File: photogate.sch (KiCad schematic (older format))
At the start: 22 parts, among them P1 CONN_01X02, P10 CONN_01X01, P11 CONN_01X01, P2 CONN_01X02, P3 CONN_01X01, P4 CONN_02X05, P5 CONN_02X04, P6 CONN_01X02, P7 CONN_02X05, P8 CONN_01X02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

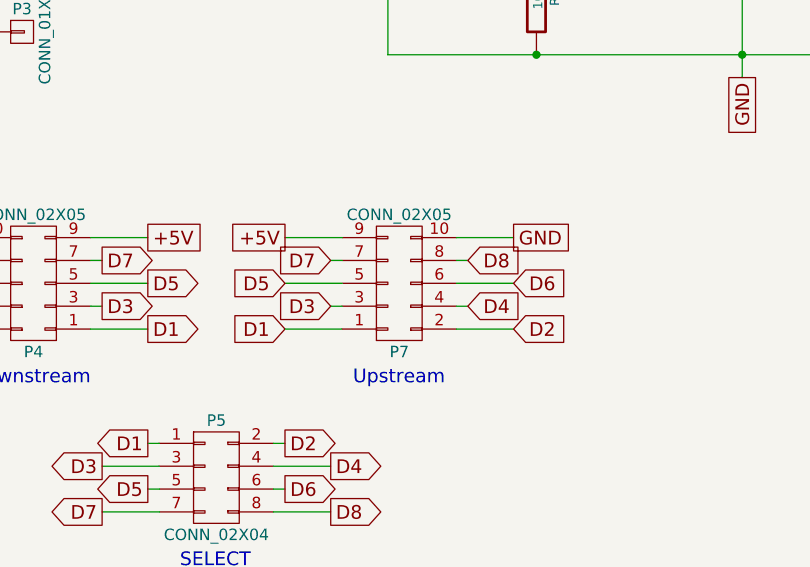
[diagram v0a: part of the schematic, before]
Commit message: Flipped flat cable connector
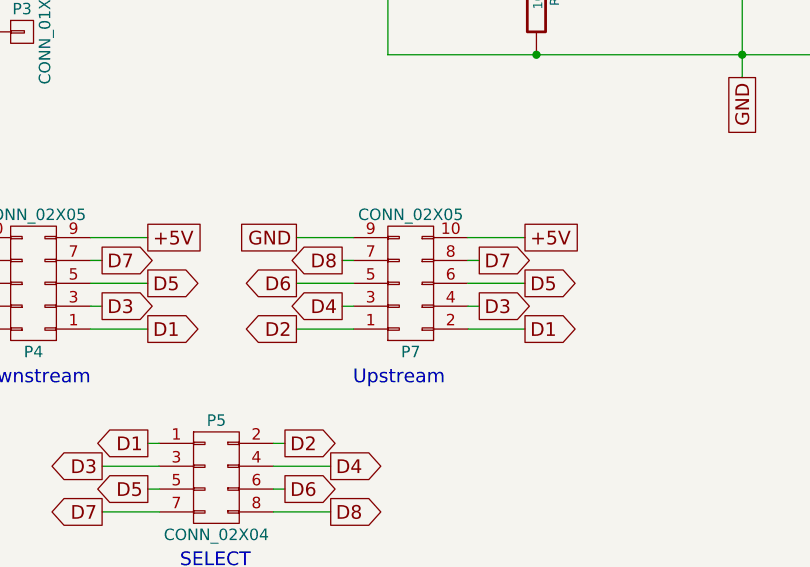
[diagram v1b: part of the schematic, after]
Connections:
- net +5V: now also P7.10 (P10); no longer P7.9 (P9)
- net D1: now also P7.2 (P2); no longer P7.1 (P1)
- net D2: now also P7.1 (P1); no longer P7.2 (P2)
- net D3: now also P7.4 (P4); no longer P7.3 (P3)
- net D4: now also P7.3 (P3); no longer P7.4 (P4)
- net D5: now also P7.6 (P6); no longer P7.5 (P5)
- net D6: now also P7.5 (P5); no longer P7.6 (P6)
- net D7: now also P7.8 (P8); no longer P7.7 (P7)
- net D8: now also P7.7 (P7); no longer P7.8 (P8)
- net GND: now also P7.9 (P9); no longer P7.10 (P10)
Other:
- moved on the sheet: P7
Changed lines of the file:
@@
 	-1   0    0    1
 $EndComp
-Text GLabel 7300 3400 2    60   UnSpc ~ 0
-GND
-Text GLabel 6300 3400 0    60   UnSpc ~ 0
-+5V
 Text GLabel 4700 3800 0    60   Output ~ 0
 D2
@@
 L CONN_02X05 P7
 U 1 1 5421918E
-P 6800 3600
-F 0 "P7" H 6800 3900 50  0000 C CNN
-F 1 "CONN_02X05" H 6800 3300 50  0000 C CNN
-F 2 "Socket_Strips:Socket_Strip_Straight_2x05" H 6800 2400 60  0001 C CNN
-F 3 "" H 6800 2400 60  0000 C CNN
-	1    6800 3600
+P 6850 3600
+F 0 "P7" H 6850 3900 50  0000 C CNN
+F 1 "CONN_02X05" H 6850 3300 50  0000 C CNN
+F 2 "Socket_Strips:Socket_Strip_Straight_2x05" H 6850 2400 60  0001 C CNN
+F 3 "" H 6850 2400 60  0000 C CNN
+	1    6850 3600
 	1    0    0    1
 $EndComp
@@
 Text GLabel 5700 3400 2    60   UnSpc ~ 0
 +5V
-Text GLabel 7300 3800 2    60   Input ~ 0
-D2
-Text GLabel 7100 3700 2    60   Input ~ 0
-D4
-Text GLabel 7300 3600 2    60   Input ~ 0
-D6
-Text GLabel 7100 3500 2    60   Input ~ 0
-D8
-Text GLabel 6300 3800 0    60   Input ~ 0
-D1
-Text GLabel 6500 3700 0    60   Input ~ 0
-D3
-Text GLabel 6300 3600 0    60   Input ~ 0
-D5
-Text GLabel 6500 3500 0    60   Input ~ 0
-D7
 Text Notes 7000 4050 2    60   ~ 0
 Upstream
@@
 Wire Wire Line
 	4900 1900 5000 1900
-Wire Wire Line
-	6500 3500 6550 3500
-Wire Wire Line
-	6300 3600 6550 3600
-Wire Wire Line
-	6550 3700 6500 3700
-Wire Wire Line
-	6300 3800 6550 3800
-Wire Wire Line
-	7100 3700 7050 3700
-Wire Wire Line
-	7300 3800 7050 3800
-Wire Wire Line
-	7050 3500 7100 3500
-Wire Wire Line
-	7300 3600 7050 3600
 Connection ~ 2800 2000
 Wire Wire Line
@@
 Wire Wire Line
 	5450 3400 5700 3400
-Wire Wire Line
-	6300 3400 6550 3400
-Wire Wire Line
-	7050 3400 7300 3400
+Text GLabel 7350 3800 2    60   Output ~ 0
+D1
+Text GLabel 7150 3700 2    60   Output ~ 0
+D3
+Text GLabel 7350 3600 2    60   Output ~ 0
+D5
+Text GLabel 7150 3500 2    60   Output ~ 0
+D7
+Text GLabel 7350 3400 2    60   UnSpc ~ 0
++5V
+Wire Wire Line
+	7100 3800 7350 3800
+Wire Wire Line
+	7100 3700 7150 3700
+Wire Wire Line
+	7100 3600 7350 3600
+Wire Wire Line
+	7100 3500 7150 3500
+Wire Wire Line
+	7100 3400 7350 3400
+Text GLabel 6350 3800 0    60   Output ~ 0
+D2
+Text GLabel 6550 3700 0    60   Output ~ 0
+D4
+Text GLabel 6350 3600 0    60   Output ~ 0
+D6
+Text GLabel 6550 3500 0    60   Output ~ 0
+D8
+Text GLabel 6350 3400 0    60   UnSpc ~ 0
+GND
+Wire Wire Line
+	6350 3600 6600 3600
+Wire Wire Line
+	6350 3800 6600 3800
+Wire Wire Line
+	6350 3400 6600 3400
+Wire Wire Line
+	6550 3500 6600 3500
+Wire Wire Line
+	6600 3700 6550 3700
 $EndSCHEMATC

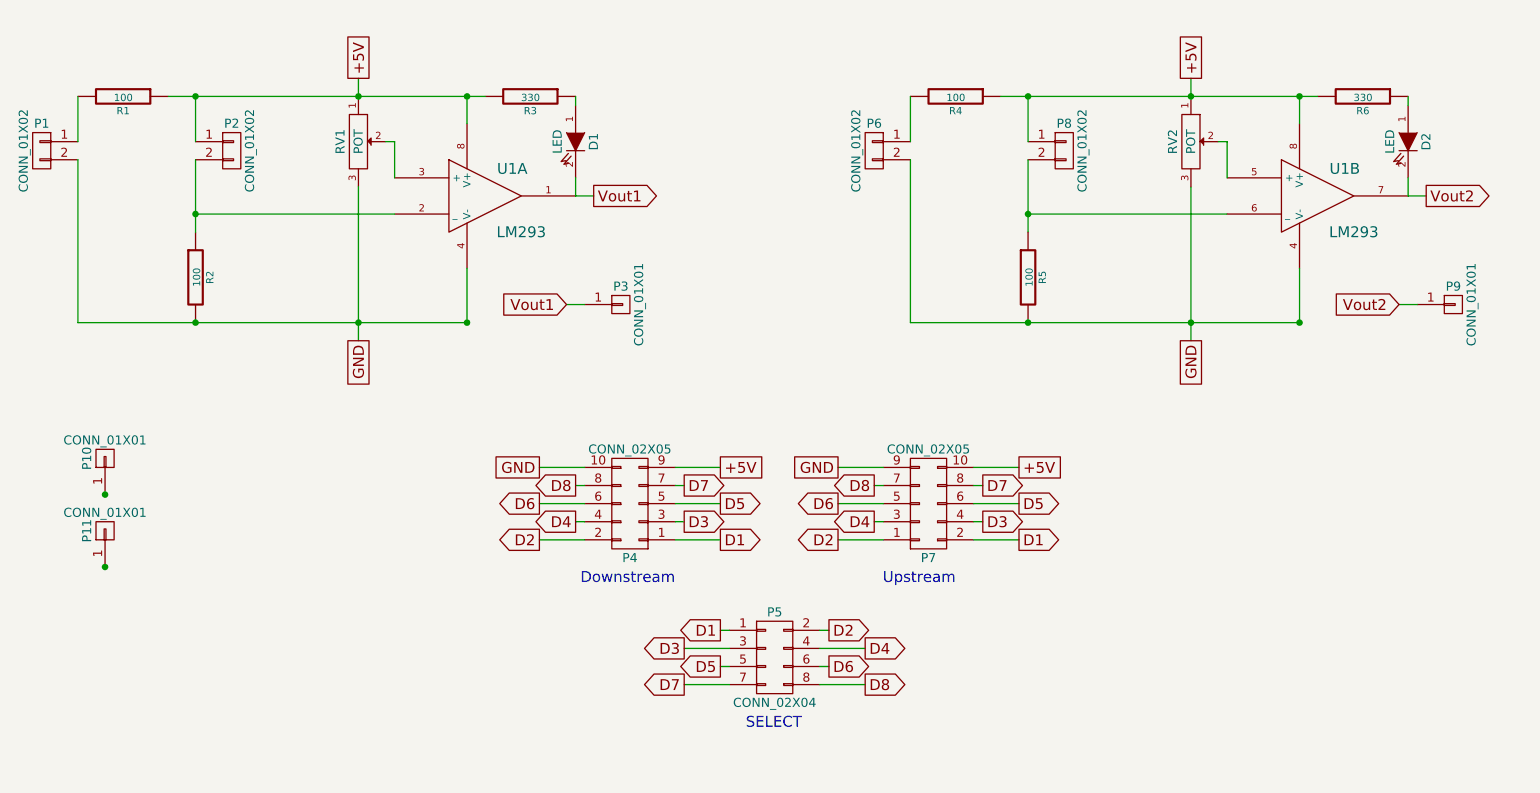
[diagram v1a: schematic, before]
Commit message: Rebuild layout w/ updated footprints
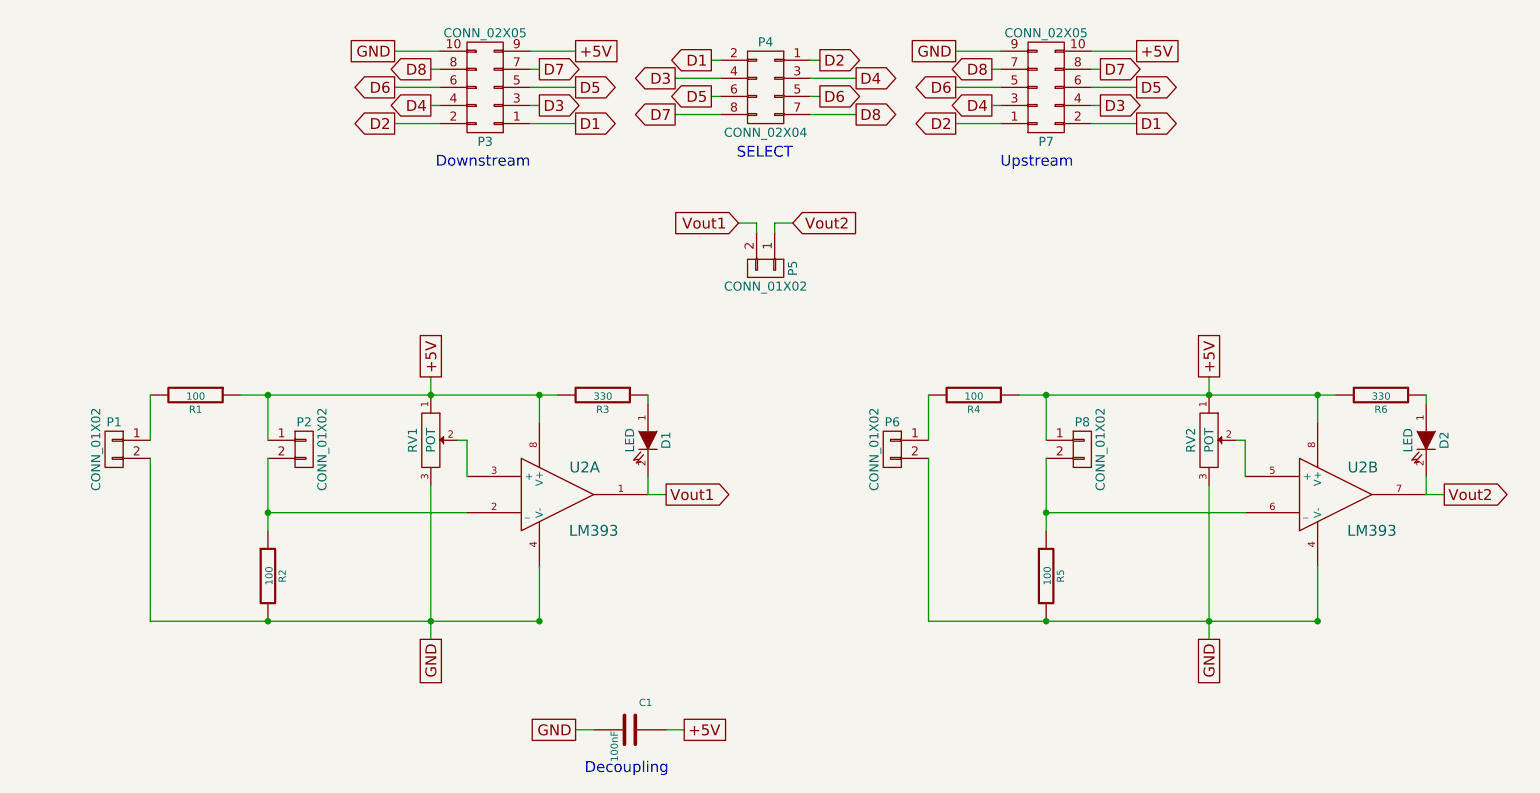
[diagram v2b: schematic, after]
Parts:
- removed P10, P11: CONN_01X01, Mounting_Holes:MountingHole_5mm, symbol CONN_01X01
- removed P3, P9: CONN_01X01, Socket_Strips:Socket_Strip_Straight_1x01, symbol CONN_01X01
- removed U1: LM293, Sockets_DIP:DIP-8__300, symbol LM293
- added C1: 100nF, SMD_Packages:SMD-1206, symbol C
- added P5: CONN_01X02, Socket_Strips:Socket_Strip_Straight_1x02, symbol CONN_01X02
- added U2: LM393, Sockets_DIP:DIP-8__300, symbol LM393
- P3: renamed from P4; footprint Socket_Strips:Socket_Strip_Straight_2x05 -> photogate_mods:Wurth_2x05_HEADER_STRAIGHT
- P7: footprint Socket_Strips:Socket_Strip_Straight_2x05 -> photogate_mods:Wurth_2x05_HEADER_STRAIGHT
- R1, R2, R3, R4, R5, R6: footprint Resistors_SMD:R_1206_HandSoldering -> Resistors_SMD:R_1206
- RV1, RV2: footprint Potentiometers:Potentiometer_Triwood_RM-065 -> photogate_mods:PVZ2A
- renumbered P5 to P4
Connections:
- net +5V: now also C1.1, U2.8 (V+), U2.8 (V+)
- net D1: now also P4.2 (P2); no longer P4.1 (P1)
- net D2: now also P4.1 (P1); no longer P4.2 (P2)
- net D3: now also P4.4 (P4); no longer P4.3 (P3)
- net D4: now also P4.3 (P3); no longer P4.4 (P4)
- net D5: now also P4.6 (P6); no longer P4.5 (P5)
- net D6: now also P4.5 (P5); no longer P4.6 (P6)
- net D7: now also P4.8 (P8); no longer P4.7 (P7)
- net D8: now also P4.7 (P7); no longer P4.8 (P8)
- net GND: now also C1.2, U2.4 (V-), U2.4 (V-)
- net Vout1: now also P5.2 (P2), U2.1
- net Vout2: now also P5.1 (P1), U2.7
- net at RV1.2: now also U2.3 (+)
- net at P2.2 (P2), R2.1: now also U2.2 (_)
- net at RV2.2: now also U2.5 (+)
- net at P8.2 (P2), R5.1: now also U2.6 (_)
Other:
- note added: "Decoupling"
- moved on the sheet: D1, D2, P1, P2, P3, P4, P6, P7, P8, R1, R2, R3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
